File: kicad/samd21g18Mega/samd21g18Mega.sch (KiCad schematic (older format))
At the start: 14 parts, among them P1 Digital, P10 CONN_01X01, P11 CONN_01X01, P12 CONN_01X01, P13 CONN_01X01, P2 Power, P3 Analog, P4 Analog, P5 PWM, P6 PWM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

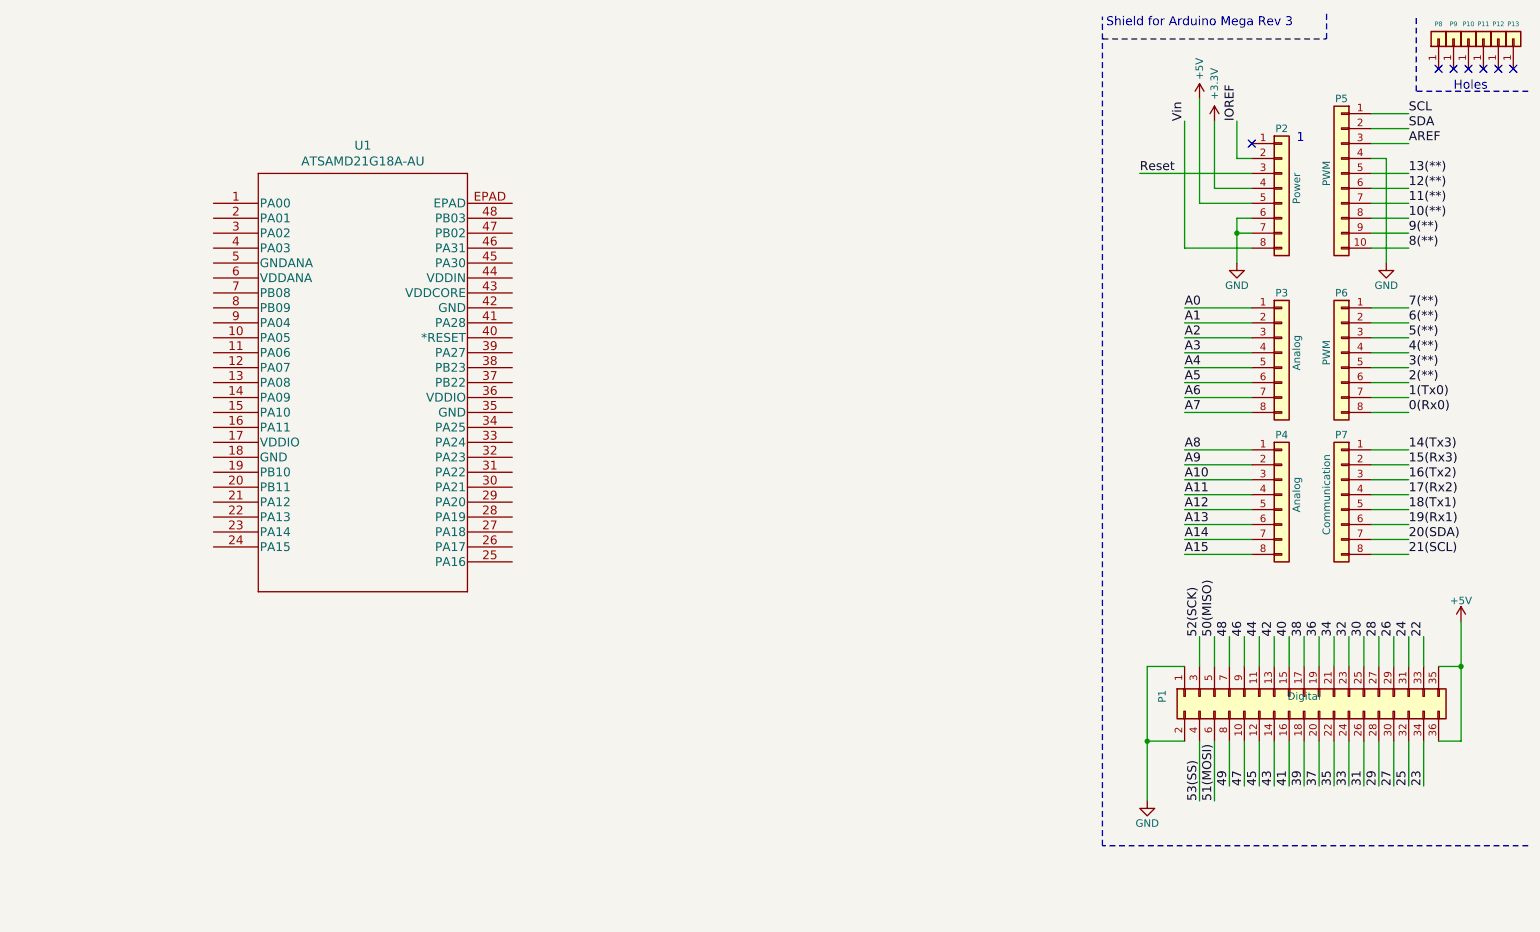
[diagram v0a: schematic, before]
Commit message: samd21 mega and whole deck cut grx
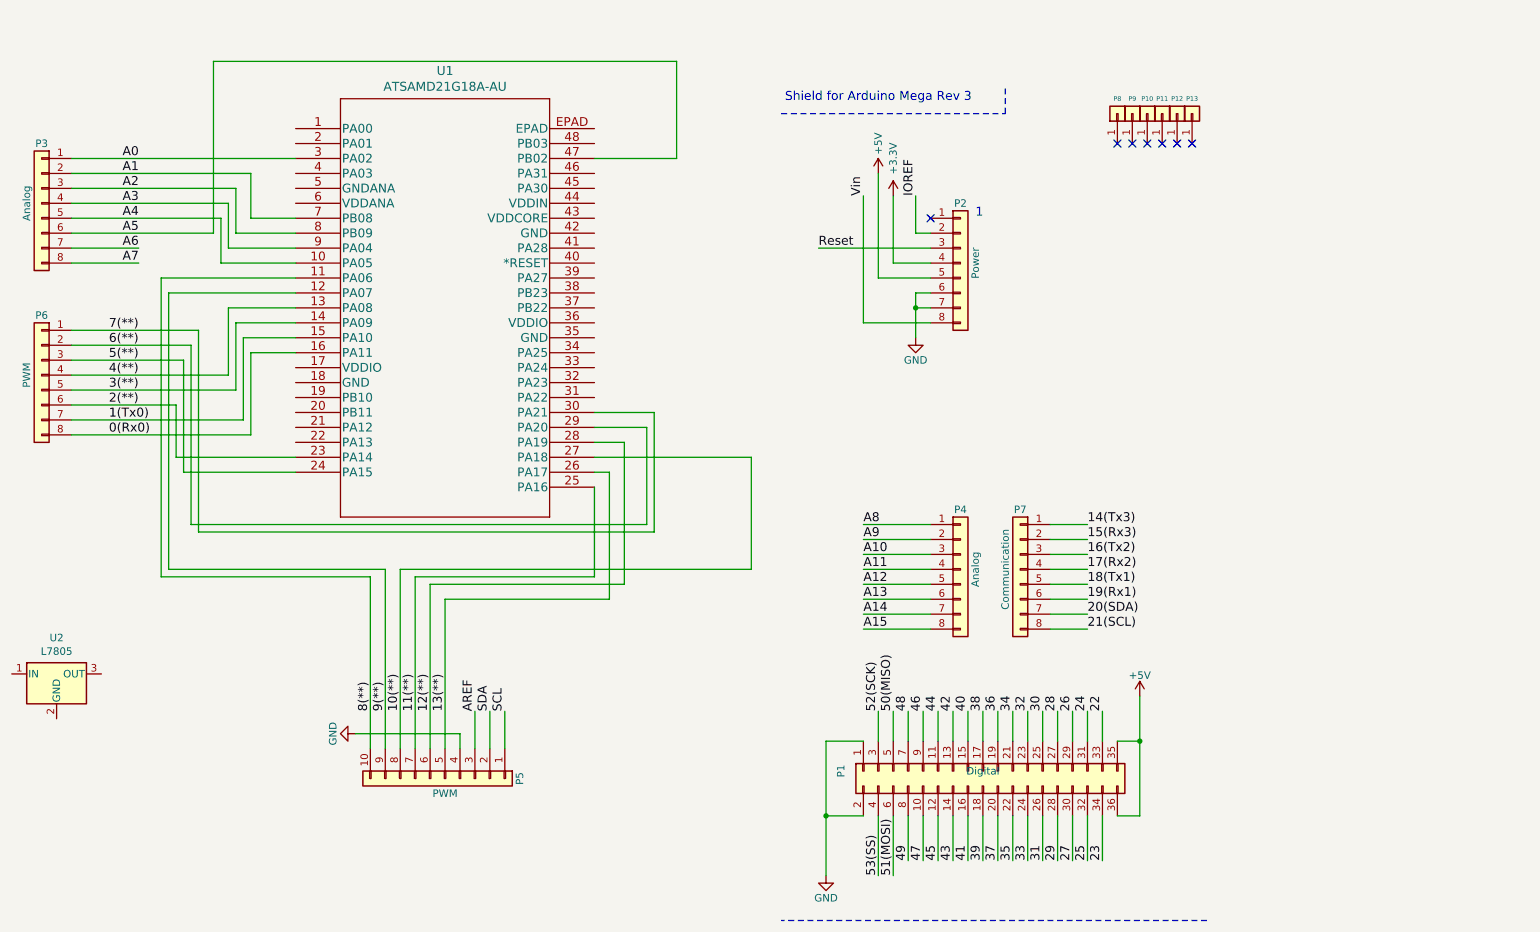
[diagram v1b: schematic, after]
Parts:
- added U2: L7805, Package_TO_SOT_THT:TO-220-3_Horizontal_TabUp, symbol Regulator_Linear:L7805
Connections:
- net 0(Rx0): now also U1.16 (PA11)
- net 1(Tx0): now also U1.15 (PA10)
- net 10(**): now also U1.27 (PA18)
- net 11(**): now also U1.25 (PA16)
- net 12(**): now also U1.28 (PA19)
- net 13(**): now also U1.26 (PA17)
- net 2(**): now also U1.23 (PA14)
- net 3(**): now also U1.14 (PA09)
- net 4(**): now also U1.13 (PA08)
- net 5(**): now also U1.24 (PA15)
- net 6(**): now also U1.29 (PA20)
- net 7(**): now also U1.30 (PA21)
- net 8(**): now also U1.11 (PA06)
- net 9(**): now also U1.12 (PA07)
- net A0: now also U1.3 (PA02)
- net A1: now also U1.7 (PB08)
- net A2: now also U1.8 (PB09)
- net A3: now also U1.9 (PA04)
- net A4: now also U1.10 (PA05)
- net A5: now also U1.47 (PB02)
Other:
- note removed: "Holes"
- moved on the sheet: P1, P10, P11, P12, P13, P2, P3, P4, P5, P6, P7, P8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

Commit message: sd21g18mega soldering guide, dealmode rough
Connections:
- net +3V3: now also U1.17 (VDDIO), U1.36 (VDDIO), U1.44 (VDDIN), U1.6 (VDDANA)
- net GND: now also U1.18 (GND), U1.35 (GND), U1.42 (GND), U1.5 (GNDANA)
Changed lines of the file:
@@
 Wire Wire Line
 	1450 2600 2300 2600
+$Comp
+L power:GND #PWR?
+U 1 1 5ECD3A18
+P 2800 3650
+F 0 "#PWR?" H 2800 3400 50  0001 C CNN
+F 1 "GND" H 2805 3477 50  0000 C CNN
+F 2 "" H 2800 3650 50  0001 C CNN
+F 3 "" H 2800 3650 50  0001 C CNN
+	1    2800 3650
+	1    0    0    -1
+$EndComp
+Wire Wire Line
+	2950 2950 2800 2950
+Wire Wire Line
+	2800 2950 2800 3650
+Wire Wire Line
+	2800 2950 2800 1650
+Wire Wire Line
+	2800 1650 2950 1650
+Connection ~ 2800 2950
+$Comp
+L power:+3.3V #PWR?
+U 1 1 5ECE43FD
+P 2850 1200
+F 0 "#PWR?" H 2850 1050 50  0001 C CNN
+F 1 "+3.3V" H 2865 1373 50  0000 C CNN
+F 2 "" H 2850 1200 50  0001 C CNN
+F 3 "" H 2850 1200 50  0001 C CNN
+	1    2850 1200
+	1    0    0    -1
+$EndComp
+Wire Wire Line
+	2850 1200 2850 1750
+Wire Wire Line
+	2850 1750 2950 1750
+Wire Wire Line
+	2850 1750 2850 2850
+Wire Wire Line
+	2850 2850 2950 2850
+Connection ~ 2850 1750
+$Comp
+L power:+3.3V #PWR?
+U 1 1 5ECF5E2D
+P 5200 1100
+F 0 "#PWR?" H 5200 950 50  0001 C CNN
+F 1 "+3.3V" H 5215 1273 50  0000 C CNN
+F 2 "" H 5200 1100 50  0001 C CNN
+F 3 "" H 5200 1100 50  0001 C CNN
+	1    5200 1100
+	1    0    0    -1
+$EndComp
+Wire Wire Line
+	5200 1100 5200 1750
+Wire Wire Line
+	5200 1750 4950 1750
+Wire Wire Line
+	5200 1750 5200 2550
+Wire Wire Line
+	5200 2550 4950 2550
+Connection ~ 5200 1750
+$Comp
+L power:GND #PWR?
+U 1 1 5ED08093
+P 5150 2950
+F 0 "#PWR?" H 5150 2700 50  0001 C CNN
+F 1 "GND" H 5155 2777 50  0000 C CNN
+F 2 "" H 5150 2950 50  0001 C CNN
+F 3 "" H 5150 2950 50  0001 C CNN
+	1    5150 2950
+	1    0    0    -1
+$EndComp
+Wire Wire Line
+	4950 2650 5150 2650
+Wire Wire Line
+	5150 2650 5150 2950
+Wire Wire Line
+	5150 2650 5150 1950
+Wire Wire Line
+	5150 1950 4950 1950
+Connection ~ 5150 2650
 $EndSCHEMATC
